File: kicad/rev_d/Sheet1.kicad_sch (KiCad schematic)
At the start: 165 parts, among them J1 JUMPER, J2 JUMPER, J3 JUMPER, J4 JUMPER, J7 JUMPER, Q1 14Mhz, X1 FDD34M, X2 IDE40M, X3 IDC26LPT, X7 DB15VGA, X8 PLB1-4I, X9 PLB1-2

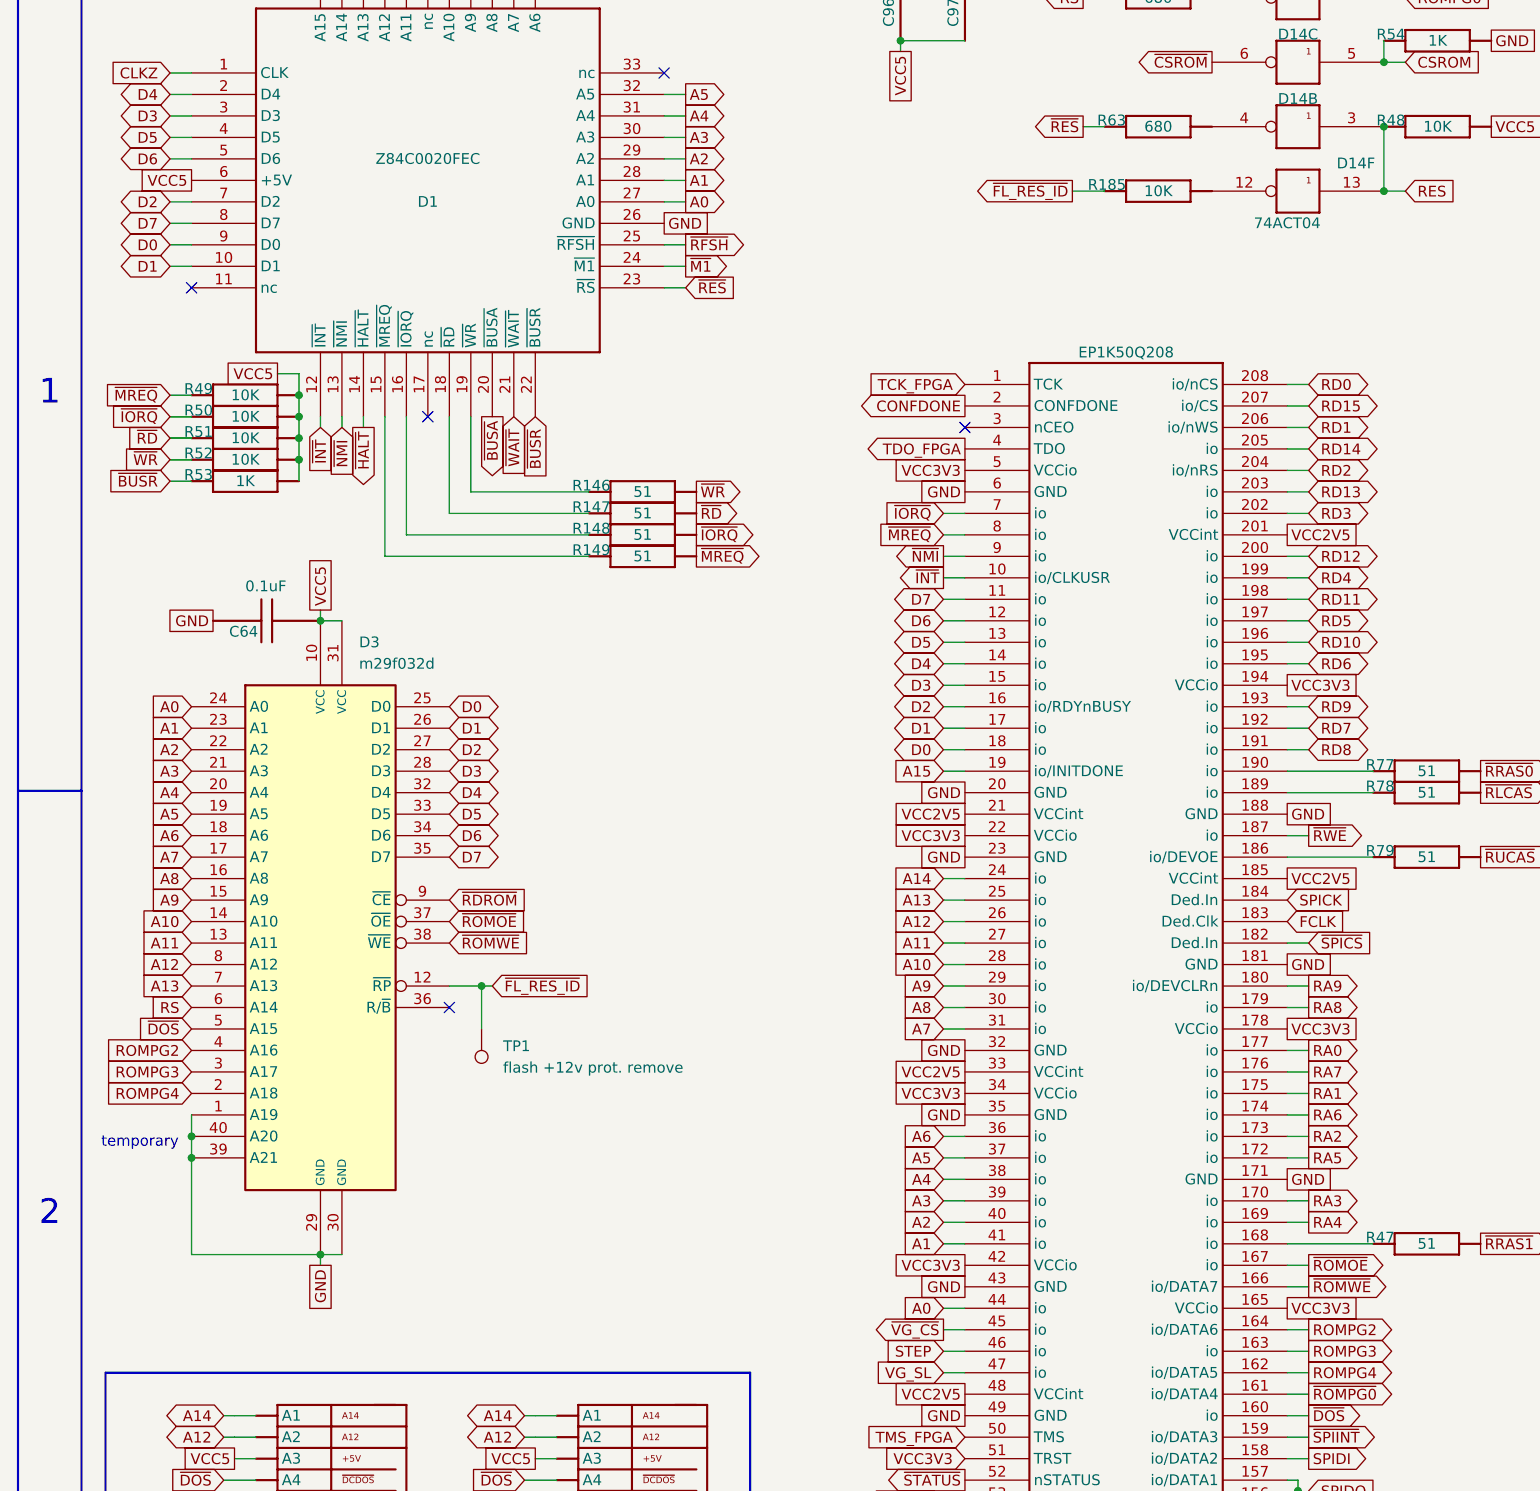
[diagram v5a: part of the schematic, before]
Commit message: pentevo: rev D: add pca9555 to control extra address pins of ROM
git-svn-id: svn://localhost/local-pentevo@1228 c6c76956-fad2-4150-a3a9-ea0a427205ba
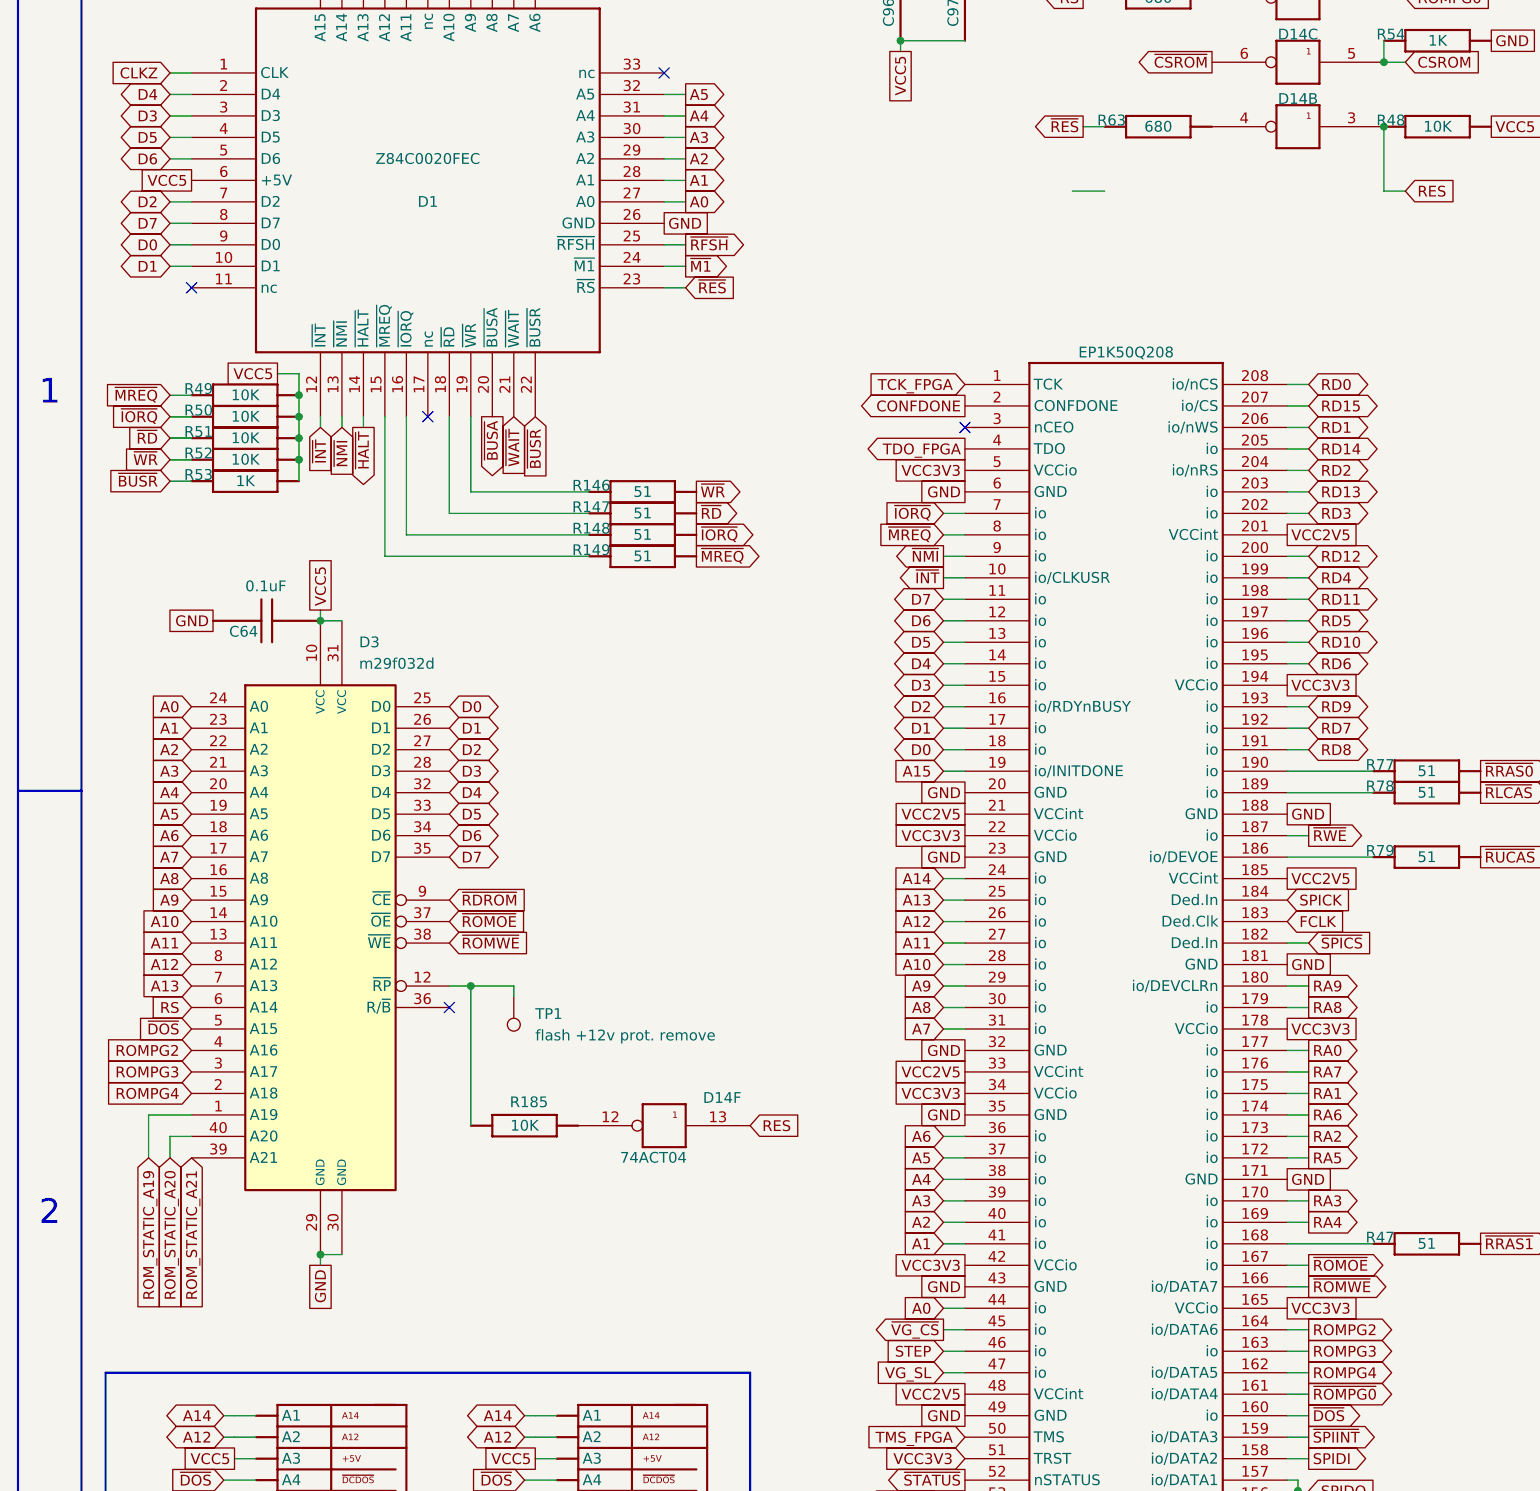
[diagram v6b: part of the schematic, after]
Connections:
- net GND: no longer D3.1 (A19), D3.39 (A21), D3.40 (A20)
- net ~{FL_RES_ID}: no longer names the net of D3.12 (~{RP}), R185.2 (i/o1), TP1.1
- new net ROM_STATIC_A19: D3.1 (A19)
- new net ROM_STATIC_A20: D3.40 (A20)
- new net ROM_STATIC_A21: D3.39 (A21)
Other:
- note removed: "temporary"
- moved on the sheet: TP1

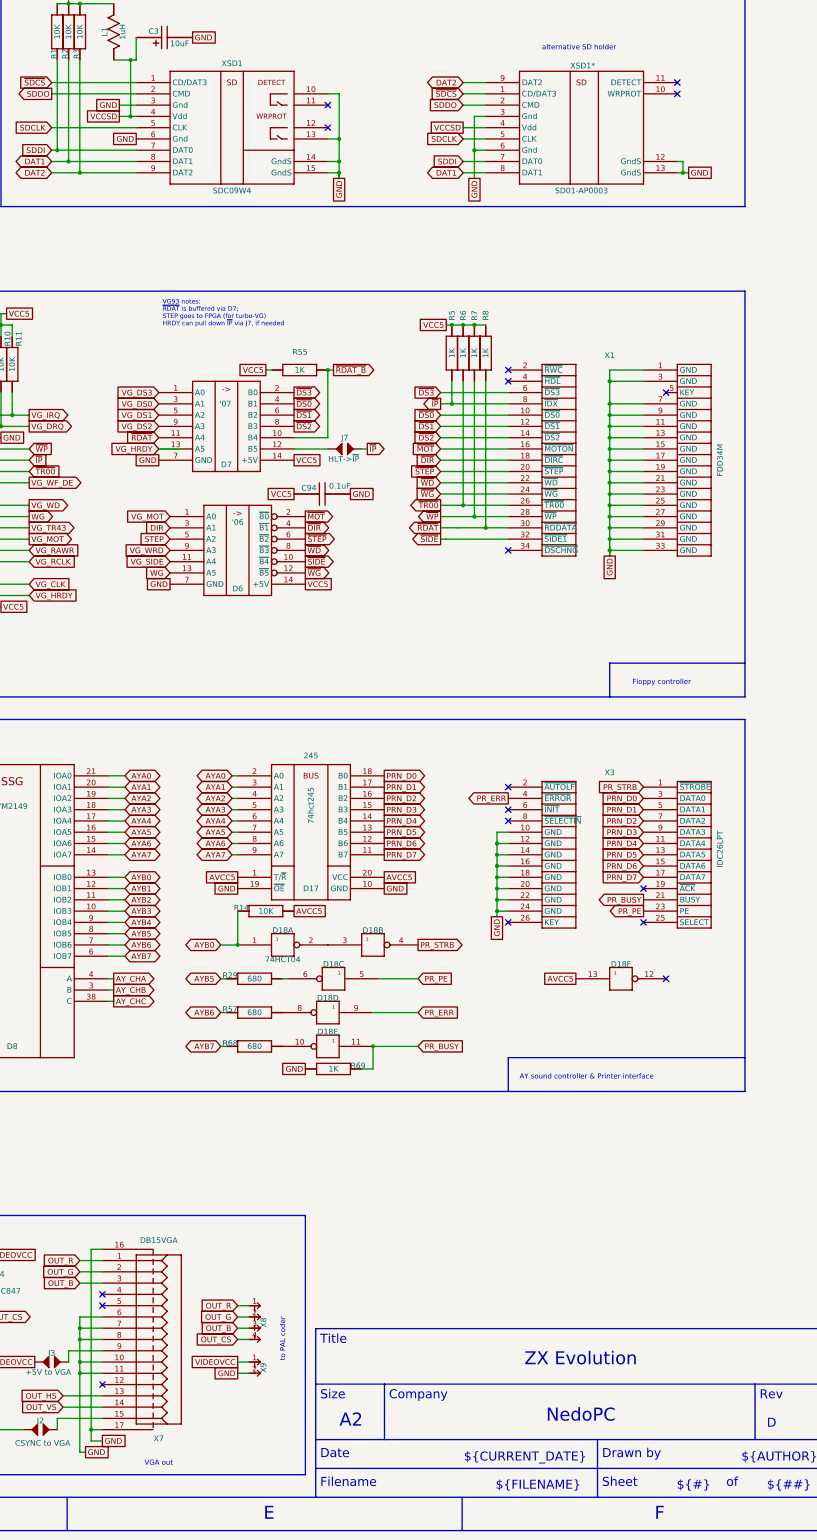
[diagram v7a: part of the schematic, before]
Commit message: pentevo: rev D: add SHIELD net, connect DB-xx shields, sdcard shields and mounting holes there
git-svn-id: svn://localhost/local-pentevo@1259 c6c76956-fad2-4150-a3a9-ea0a427205ba
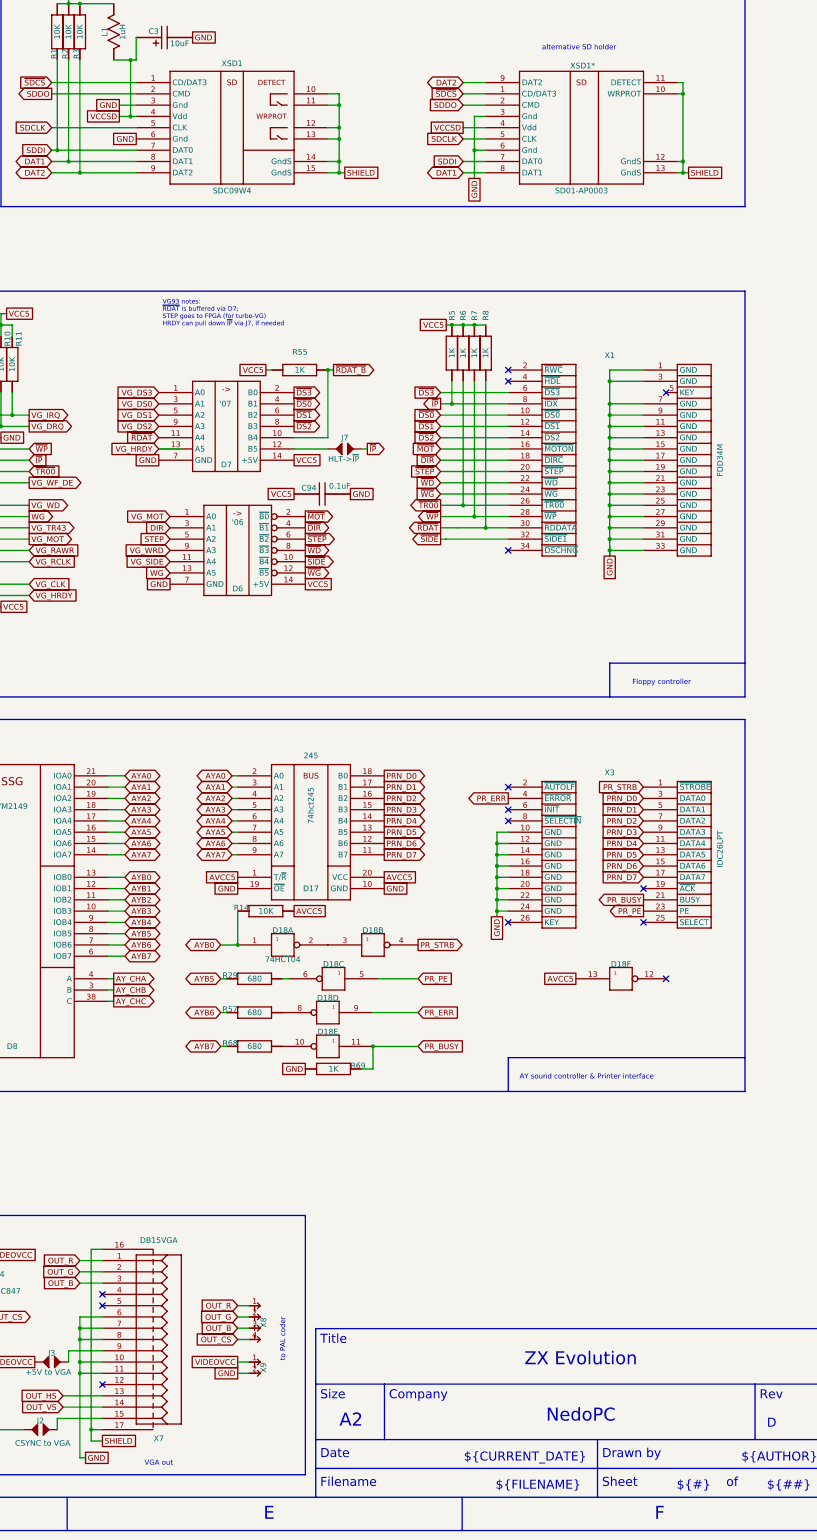
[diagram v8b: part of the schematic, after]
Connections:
- net GND: no longer X7.16, X7.17, XSD1*.12 (GndS), XSD1*.13 (GndS), XSD1.10 (DETECT), XSD1.13 (WRPROT), XSD1.14 (GndS), XSD1.15 (GndS)
- net SHIELD: now reaches XSD1.11 (DETECT)
- net SHIELD: now also X7.16, X7.17, XSD1*.10 (WRPROT), XSD1*.11 (DETECT), XSD1*.12 (GndS), XSD1*.13 (GndS), XSD1.10 (DETECT), XSD1.12 (WRPROT), XSD1.13 (WRPROT), XSD1.14 (GndS), XSD1.15 (GndS)
- no-connect marks 68 -> 64
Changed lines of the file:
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@@
 	)
 	(junction
+		(at 429.26 97.79)
+		(diameter 0)
+		(color 0 0 0 0)
+	)
+	(junction
 		(at 490.22 177.8)
 		(diameter 0)
@@
 	)
 	(junction
+		(at 506.73 110.49)
+		(diameter 0)
+		(color 0 0 0 0)
+	)
+	(junction
 		(at 302.26 60.96)
 		(diameter 0)
@@
 	)
 	(junction
+		(at 429.26 113.03)
+		(diameter 0)
+		(color 0 0 0 0)
+	)
+	(junction
 		(at 217.17 227.33)
 		(diameter 0)
@@
 	)
 	(junction
+		(at 506.73 95.25)
+		(diameter 0)
+		(color 0 0 0 0)
+	)
+	(junction
 		(at 294.64 73.66)
 		(diameter 0)
@@
 	)
 	(junction
-		(at 429.26 113.03)
+		(at 464.82 279.4)
 		(diameter 0)
 		(color 0 0 0 0)
 	)
 	(junction
-		(at 464.82 279.4)
+		(at 166.37 392.43)
 		(diameter 0)
 		(color 0 0 0 0)
 	)
 	(junction
-		(at 166.37 392.43)
+		(at 293.37 237.49)
 		(diameter 0)
 		(color 0 0 0 0)
 	)
 	(junction
-		(at 293.37 237.49)
+		(at 429.26 102.87)
 		(diameter 0)
 		(color 0 0 0 0)
@@
 	)
 	(no_connect
-		(at 505.46 95.25)
-	)
-	(no_connect
 		(at 375.92 368.3)
 	)
@@
 	)
 	(no_connect
-		(at 505.46 92.71)
-	)
-	(no_connect
-		(at 426.72 97.79)
-	)
-	(no_connect
 		(at 73.66 375.92)
 	)
@@
 	)
 	(no_connect
-		(at 426.72 102.87)
-	)
-	(no_connect
 		(at 38.1 307.34)
 	)
@@
 		)
 	)
-	(wire
-		(pts
-			(xy 429.26 114.3) (xy 429.26 113.03)
-		)
-		(stroke
-			(width 0.0508)
-			(type default)
-		)
-	)
 	(polyline
 		(pts
@@
 	(wire
 		(pts
+			(xy 506.73 95.25) (xy 506.73 110.49)
+		)
+		(stroke
+			(width 0)
+			(type default)
+		)
+	)
+	(wire
+		(pts
 			(xy 359.41 177.8) (xy 347.98 177.8)
 		)
@@
 	(wire
 		(pts
+			(xy 505.46 95.25) (xy 506.73 95.25)
+		)
+		(stroke
+			(width 0)
+			(type default)
+		)
+	)
+	(wire
+		(pts
 			(xy 119.38 157.48) (xy 121.92 157.48)
 		)
@@
 	(wire
 		(pts
+			(xy 429.26 102.87) (xy 429.26 97.79)
+		)
+		(stroke
+			(width 0)
+			(type default)
+		)
+	)
+	(wire
+		(pts
 			(xy 353.06 147.32) (xy 355.6 147.32)
 		)
@@
 	(wire
 		(pts
-			(xy 370.84 401.32) (xy 370.84 383.54)
+			(xy 370.84 402.59) (xy 370.84 383.54)
 		)
 		(stroke
@@
 	(wire
 		(pts
-			(xy 429.26 114.3) (xy 429.26 113.03)
+			(xy 453.39 195.58) (xy 467.36 195.58)
 		)
 		(stroke
@@
 	(wire
 		(pts
-			(xy 453.39 195.58) (xy 467.36 195.58)
+			(xy 130.81 39.37) (xy 133.35 39.37)
 		)
 		(stroke
@@
 	(wire
 		(pts
-			(xy 130.81 39.37) (xy 133.35 39.37)
+			(xy 119.38 332.74) (xy 121.92 332.74)
 		)
 		(stroke
@@
 	(wire
 		(pts
-			(xy 119.38 332.74) (xy 121.92 332.74)
+			(xy 429.26 97.79) (xy 429.26 95.25)
 		)
 		(stroke
@@
 	(wire
 		(pts
+			(xy 426.72 102.87) (xy 429.26 102.87)
+		)
+		(stroke
+			(width 0)
+			(type default)
+		)
+	)
+	(wire
+		(pts
 			(xy 119.38 246.38) (xy 121.92 246.38)
 		)
@@
 	(wire
 		(pts
+			(xy 429.26 113.03) (xy 430.53 113.03)
+		)
+		(stroke
+			(width 0)
+			(type default)
+		)
+	)
+	(wire
+		(pts
 			(xy 119.38 243.84) (xy 121.92 243.84)
 		)
@@
 	(wire
 		(pts
-			(xy 429.26 113.03) (xy 426.72 113.03)
+			(xy 426.72 113.03) (xy 429.26 113.03)
 		)
 		(stroke
@@
 	(wire
 		(pts
-			(xy 429.26 105.41) (xy 429.26 95.25)
+			(xy 429.26 105.41) (xy 429.26 102.87)
 		)
 		(stroke
@@
 	(wire
 		(pts
+			(xy 426.72 97.79) (xy 429.26 97.79)
+		)
+		(stroke
+			(width 0)
+			(type default)
+		)
+	)
+	(wire
+		(pts
 			(xy 274.32 386.08) (xy 271.78 386.08)
 		)
@@
 	(wire
 		(pts
+			(xy 506.73 92.71) (xy 506.73 95.25)
+		)
+		(stroke
+			(width 0)
+			(type default)
+		)
+	)
+	(wire
+		(pts
 			(xy 162.56 134.62) (xy 160.02 134.62)
 		)
@@
 	(wire
 		(pts
+			(xy 505.46 92.71) (xy 506.73 92.71)
+		)
+		(stroke
+			(width 0)
+			(type default)
+		)
+	)
+	(wire
+		(pts
 			(xy 274.32 388.62) (xy 271.78 388.62)
 		)
@@
 	(wire
 		(pts
-			(xy 372.11 401.32) (xy 370.84 401.32)
+			(xy 372.11 402.59) (xy 370.84 402.59)
 		)
 		(stroke
@@
 		)
 	)
+	(global_label "SHIELD"
+		(shape passive)
+		(at 375.92 398.78 0)
+		(fields_autoplaced yes)
+		(effects
+			(font
+				(size 1.27 1.27)
+			)
+			(justify left)
+		)
+		(property "Intersheetrefs" "${INTERSHEET_REFS}"
+			(at 384.3858 398.78 0)
+			(effects
+				(font
+					(size 1.27 1.27)
+				)
+				(justify left)
+				(hide yes)
+			)
+		)
+	)
 	(global_label "VCC5"
 		(shape passive)
@@
 	(global_label "GND"
 		(shape passive)
-		(at 372.11 401.32 0)
+		(at 372.11 402.59 0)
 		(fields_autoplaced yes)
 		(effects
@@
 		)
 		(property "Intersheetrefs" "${INTERSHEET_REFS}"
-			(at 377.8544 401.32 0)
+			(at 377.8544 402.59 0)
 			(effects
 				(font
@@
 	(global_label "GND"
 		(shape passive)
-		(at 508 113.03 0)
+		(at 267.97 93.98 0)
 		(fields_autoplaced yes)
 		(effects
@@
 		)
 		(property "Intersheetrefs" "${INTERSHEET_REFS}"
-			(at 513.7444 113.03 0)
+			(at 273.7144 93.98 0)
 			(effects
 				(font
@@
 		)
 	)
-	(global_label "GND"
-		(shape passive)
-		(at 267.97 93.98 0)
+	(global_label "~{RWE}"
+		(shape input)
+		(at 227.33 111.76 180)
 		(fields_autoplaced yes)
 		(effects
@@
 				(size 1.27 1.27)
 			)
-			(justify left)
+			(justify right)
 		)
 		(property "Intersheetrefs" "${INTERSHEET_REFS}"
-			(at 273.7144 93.98 0)
+			(at 220.4744 111.76 0)
 			(effects
 				(font
 					(size 1.27 1.27)
 				)
-				(justify left)
+				(justify right)
 				(hide yes)
 			)
 		)
 	)
-	(global_label "~{RWE}"
-		(shape input)
-		(at 227.33 111.76 180)
+	(global_label "SHIELD"
+		(shape passive)
+		(at 508 113.03 0)
 		(fields_autoplaced yes)
 		(effects
@@
 				(size 1.27 1.27)
 			)
-			(justify right)
+			(justify left)
 		)
 		(property "Intersheetrefs" "${INTERSHEET_REFS}"
-			(at 220.4744 111.76 0)
+			(at 516.4658 113.03 0)
 			(effects
 				(font
 					(size 1.27 1.27)
 				)
-				(justify right)
+				(justify left)
 				(hide yes)
 			)
@@
 		)
 	)
-	(global_label "GND"
-		(shape passive)
-		(at 429.26 114.3 270)
-		(fields_autoplaced yes)
-		(effects
-			(font
-				(size 1.27 1.27)
-			)
-			(justify right)
-		)
-		(property "Intersheetrefs" "${INTERSHEET_REFS}"
-			(at 429.26 120.0444 90)
-			(effects
-				(font
-					(size 1.27 1.27)
-				)
-				(justify right)
-				(hide yes)
-			)
-		)
-	)
 	(global_label "RD13"
 		(shape bidirectional)
@@
 	(global_label "GND"
 		(shape passive)
-		(at 375.92 398.78 0)
-		(fields_autoplaced yes)
-		(effects
-			(font
-				(size 1.27 1.27)
-			)
-			(justify left)
-		)
-		(property "Intersheetrefs" "${INTERSHEET_REFS}"
-			(at 381.6644 398.78 0)
-			(effects
-				(font
-					(size 1.27 1.27)
-				)
-				(justify left)
-				(hide yes)
-			)
-		)
-	)
-	(global_label "GND"
-		(shape passive)
 		(at 71.12 228.6 180)
 		(fields_autoplaced yes)
@@
 			(effects
 				(font
+					(size 1.27 1.27)
+				)
+				(justify left)
+				(hide yes)
+			)
+		)
+	)
+	(global_label "SHIELD"
+		(shape passive)
+		(at 430.53 113.03 0)
+		(fields_autoplaced yes)
+		(effects
+			(font
+				(size 1.27 1.27)
+			)
+			(justify left)
+		)
+		(property "Intersheetrefs" "${INTERSHEET_REFS}"
+			(at 438.9958 113.03 0)
+			(effects
+				(font
